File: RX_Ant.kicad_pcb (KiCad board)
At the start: 2 copper layers, 100 x 100 mm, 1705 parts, among them J1 CONN_COAXIAL, J10 CONN_COAXIAL, J11 CONN_01X06, J12 CONN_01X05, J13 CONN_COAXIAL, J14 CONN_COAXIAL, J15 CONN_COAXIAL, J16 CONN_01X01, J17 CONN_01X01, J18 CONN_01X01, J19 CONN_01X01, J2 CONN_COAXIAL, J20 CONN_01X01, J21 CONN_01X01, J22 CONN_01X01, J23 CONN_01X01, J24 CONN_COAXIAL, J25 CONN_COAXIAL, J26 CONN_COAXIAL, J27 CONN_COAXIAL, J28 CONN_COAXIAL, J29 CONN_COAXIAL, J3 CONN_COAXIAL, J30 CONN_COAXIAL, J31 CONN_COAXIAL, J32 CONN_COAXIAL, J33 CONN_COAXIAL, J34 CONN_COAXIAL, J35 CONN_COAXIAL, J36 CONN_COAXIAL, J4 CONN_COAXIAL, J5 CONN_COAXIAL, J6 CONN_COAXIAL, J7 CONN_COAXIAL, J8 CONN_COAXIAL, J9 CONN_COAXIAL

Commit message: stiching again, new gerber
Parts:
- removed the REF** at (117.0, 113.0)
- removed the REF** at (116.0, 113.0)
- removed the REF** at (117.0, 112.0)
- removed the REF** at (116.0, 112.0)
- removed the REF** at (117.0, 111.0)
- removed the REF** at (116.0, 111.0)
- removed the REF** at (115.0, 113.0)
- removed the REF** at (114.0, 113.0)
- removed the REF** at (113.0, 113.0)
- removed the REF** at (112.0, 113.0)
- removed the REF** at (111.0, 113.0)
- removed the REF** at (110.0, 113.0)
- removed the REF** at (109.0, 113.0)
- removed the REF** at (115.0, 112.0)
- removed the REF** at (114.0, 112.0)
- removed the REF** at (113.0, 112.0)
- removed the REF** at (112.0, 112.0)
- removed the REF** at (111.0, 112.0)
- removed the REF** at (110.0, 112.0)
- removed the REF** at (109.0, 112.0)
- removed the REF** at (115.0, 111.0)
- removed the REF** at (114.0, 111.0)
- removed the REF** at (113.0, 111.0)
- removed the REF** at (112.0, 111.0)
- removed the REF** at (111.0, 111.0)
- removed the REF** at (110.0, 111.0)
- removed the REF** at (109.0, 111.0)
- removed the REF** at (101.0, 113.0)
- removed the REF** at (100.0, 113.0)
- removed the REF** at (99.0, 113.0)
- removed the REF** at (98.0, 113.0)
- removed the REF** at (97.0, 113.0)
- removed the REF** at (96.0, 113.0)
- removed the REF** at (95.0, 113.0)
- removed the REF** at (94.0, 113.0)
- removed the REF** at (101.0, 112.0)
- removed the REF** at (100.0, 112.0)
- removed the REF** at (99.0, 112.0)
- removed the REF** at (98.0, 112.0)
- removed the REF** at (97.0, 112.0)
- removed the REF** at (96.0, 112.0)
- removed the REF** at (95.0, 112.0)
- removed the REF** at (94.0, 112.0)
- removed the REF** at (101.0, 111.0)
- removed the REF** at (100.0, 111.0)
- removed the REF** at (99.0, 111.0)
- removed the REF** at (98.0, 111.0)
- removed the REF** at (97.0, 111.0)
- removed the REF** at (96.0, 111.0)
- removed the REF** at (95.0, 111.0)
- removed the REF** at (94.0, 111.0)
- removed the REF** at (86.0, 113.0)
- removed the REF** at (85.0, 113.0)
- removed the REF** at (84.0, 113.0)
- removed the REF** at (83.0, 113.0)
- removed the REF** at (82.0, 113.0)
- removed the REF** at (81.0, 113.0)
- removed the REF** at (80.0, 113.0)
- removed the REF** at (79.0, 113.0)
- removed the REF** at (86.0, 112.0)
- removed the REF** at (85.0, 112.0)
- removed the REF** at (84.0, 112.0)
- removed the REF** at (83.0, 112.0)
- removed the REF** at (82.0, 112.0)
- removed the REF** at (81.0, 112.0)
- removed the REF** at (80.0, 112.0)
- removed the REF** at (79.0, 112.0)
- removed the REF** at (86.0, 111.0)
- removed the REF** at (85.0, 111.0)
- removed the REF** at (84.0, 111.0)
- removed the REF** at (83.0, 111.0)
- removed the REF** at (82.0, 111.0)
- removed the REF** at (81.0, 111.0)
- removed the REF** at (80.0, 111.0)
- removed the REF** at (79.0, 111.0)
- removed the REF** at (71.0, 113.0)
- removed the REF** at (70.0, 113.0)
- removed the REF** at (69.0, 113.0)
- removed the REF** at (68.0, 113.0)
- removed the REF** at (67.0, 113.0)
- removed the REF** at (66.0, 113.0)
- removed the REF** at (65.0, 113.0)
- removed the REF** at (64.0, 113.0)
- removed the REF** at (71.0, 112.0)
- removed the REF** at (70.0, 112.0)
- removed the REF** at (69.0, 112.0)
- removed the REF** at (68.0, 112.0)
- removed the REF** at (67.0, 112.0)
- removed the REF** at (66.0, 112.0)
- removed the REF** at (65.0, 112.0)
- removed the REF** at (64.0, 112.0)
- removed the REF** at (71.0, 111.0)
- removed the REF** at (70.0, 111.0)
- removed the REF** at (69.0, 111.0)
- removed the REF** at (68.0, 111.0)
- removed the REF** at (67.0, 111.0)
- removed the REF** at (66.0, 111.0)
- removed the REF** at (65.0, 111.0)
- removed the REF** at (64.0, 111.0)
- removed the REF** at (56.0, 113.0)
- removed the REF** at (55.0, 113.0)
- removed the REF** at (54.0, 113.0)
- removed the REF** at (53.0, 113.0)
- removed the REF** at (52.0, 113.0)
- removed the REF** at (51.0, 113.0)
- removed the REF** at (50.0, 113.0)
- removed the REF** at (49.0, 113.0)
- removed the REF** at (56.0, 112.0)
- removed the REF** at (55.0, 112.0)
- removed the REF** at (54.0, 112.0)
- removed the REF** at (53.0, 112.0)
- removed the REF** at (52.0, 112.0)
- removed the REF** at (51.0, 112.0)
- removed the REF** at (50.0, 112.0)
- removed the REF** at (49.0, 112.0)
- removed the REF** at (56.0, 111.0)
- removed the REF** at (55.0, 111.0)
- removed the REF** at (54.0, 111.0)
- removed the REF** at (53.0, 111.0)
- removed the REF** at (52.0, 111.0)
- removed the REF** at (51.0, 111.0)
- removed the REF** at (50.0, 111.0)
- removed the REF** at (49.0, 111.0)
- removed the REF** at (41.0, 113.0)
- removed the REF** at (40.0, 113.0)
- removed the REF** at (39.0, 113.0)
- removed the REF** at (38.0, 113.0)
- removed the REF** at (37.0, 113.0)
- removed the REF** at (36.0, 113.0)
- removed the REF** at (35.0, 113.0)
- removed the REF** at (34.0, 113.0)
- removed the REF** at (33.0, 113.0)
- removed the REF** at (32.0, 113.0)
- removed the REF** at (31.0, 113.0)
- removed the REF** at (30.0, 113.0)
- removed the REF** at (29.0, 113.0)
- removed the REF** at (28.0, 113.0)
- removed the REF** at (27.0, 113.0)
- removed the REF** at (41.0, 112.0)
- removed the REF** at (40.0, 112.0)
- removed the REF** at (39.0, 112.0)
- removed the REF** at (38.0, 112.0)
- removed the REF** at (37.0, 112.0)
- removed the REF** at (36.0, 112.0)
- removed the REF** at (35.0, 112.0)
- removed the REF** at (34.0, 112.0)
- removed the REF** at (33.0, 112.0)
- removed the REF** at (32.0, 112.0)
- removed the REF** at (31.0, 112.0)
- removed the REF** at (30.0, 112.0)
- removed the REF** at (29.0, 112.0)
- removed the REF** at (28.0, 112.0)
- removed the REF** at (27.0, 112.0)
- removed the REF** at (41.0, 111.0)
- removed the REF** at (40.0, 111.0)
- removed the REF** at (39.0, 111.0)
- removed the REF** at (38.0, 111.0)
- removed the REF** at (37.0, 111.0)
- removed the REF** at (36.0, 111.0)
- removed the REF** at (35.0, 111.0)
- removed the REF** at (34.0, 111.0)
- removed the REF** at (33.0, 111.0)
- removed the REF** at (32.0, 111.0)
- removed the REF** at (31.0, 111.0)
- removed the REF** at (30.0, 111.0)
- removed the REF** at (29.0, 111.0)
- removed the REF** at (28.0, 111.0)
- removed the REF** at (27.0, 111.0)

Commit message: stiching again, new gerber
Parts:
- added REF**: via, via:via, F.Cu at (111.0, 124.0)
- added REF**: via, via:via, F.Cu at (83.0, 124.0)
- added REF**: via, via:via, F.Cu at (82.0, 124.0)
- added REF**: via, via:via, F.Cu at (81.0, 124.0)
- added REF**: via, via:via, F.Cu at (84.0, 123.0)
- added REF**: via, via:via, F.Cu at (83.0, 123.0)
- added REF**: via, via:via, F.Cu at (82.0, 123.0)
- added REF**: via, via:via, F.Cu at (69.0, 124.0)
- added REF**: via, via:via, F.Cu at (68.0, 124.0)
- added REF**: via, via:via, F.Cu at (67.0, 124.0)
- added REF**: via, via:via, F.Cu at (66.0, 124.0)
- added REF**: via, via:via, F.Cu at (99.0, 124.0)
- added REF**: via, via:via, F.Cu at (69.0, 123.0)
- added REF**: via, via:via, F.Cu at (68.0, 123.0)
- added REF**: via, via:via, F.Cu at (67.0, 123.0)
- added REF**: via, via:via, F.Cu at (54.0, 124.0)
- added REF**: via, via:via, F.Cu at (53.0, 124.0)
- added REF**: via, via:via, F.Cu at (52.0, 124.0)
- added REF**: via, via:via, F.Cu at (51.0, 124.0)
- added REF**: via, via:via, F.Cu at (54.0, 123.0)
- added REF**: via, via:via, F.Cu at (53.0, 123.0)
- added REF**: via, via:via, F.Cu at (52.0, 123.0)
- added REF**: via, via:via, F.Cu at (98.0, 124.0)
- added REF**: via, via:via, F.Cu at (38.0, 124.0)
- added REF**: via, via:via, F.Cu at (37.0, 124.0)
- added REF**: via, via:via, F.Cu at (36.0, 124.0)
- added REF**: via, via:via, F.Cu at (35.0, 124.0)
- added REF**: via, via:via, F.Cu at (34.0, 124.0)
- added REF**: via, via:via, F.Cu at (33.0, 124.0)
- added REF**: via, via:via, F.Cu at (32.0, 124.0)
- added REF**: via, via:via, F.Cu at (31.0, 124.0)
- added REF**: via, via:via, F.Cu at (30.0, 124.0)
- added REF**: via, via:via, F.Cu at (29.0, 124.0)
- added REF**: via, via:via, F.Cu at (97.0, 124.0)
- added REF**: via, via:via, F.Cu at (38.0, 123.0)
- added REF**: via, via:via, F.Cu at (37.0, 123.0)
- added REF**: via, via:via, F.Cu at (36.0, 123.0)
- added REF**: via, via:via, F.Cu at (35.0, 123.0)
- added REF**: via, via:via, F.Cu at (34.0, 123.0)
- added REF**: via, via:via, F.Cu at (33.0, 123.0)
- added REF**: via, via:via, F.Cu at (32.0, 123.0)
- added REF**: via, via:via, F.Cu at (31.0, 123.0)
- added REF**: via, via:via, F.Cu at (30.0, 123.0)
- added REF**: via, via:via, F.Cu at (111.0, 123.0)
- added REF**: via, via:via, F.Cu at (96.0, 124.0)
- added REF**: via, via:via, F.Cu at (96.0, 123.0)
- added REF**: via, via:via, F.Cu at (81.0, 123.0)
- added REF**: via, via:via, F.Cu at (66.0, 123.0)
- added REF**: via, via:via, F.Cu at (51.0, 123.0)
- added REF**: via, via:via, F.Cu at (29.0, 123.0)
- added REF**: via, via:via, F.Cu at (99.0, 123.0)
- added REF**: via, via:via, F.Cu at (98.0, 123.0)
- added REF**: via, via:via, F.Cu at (97.0, 123.0)
- added REF**: via, via:via, F.Cu at (84.0, 124.0)

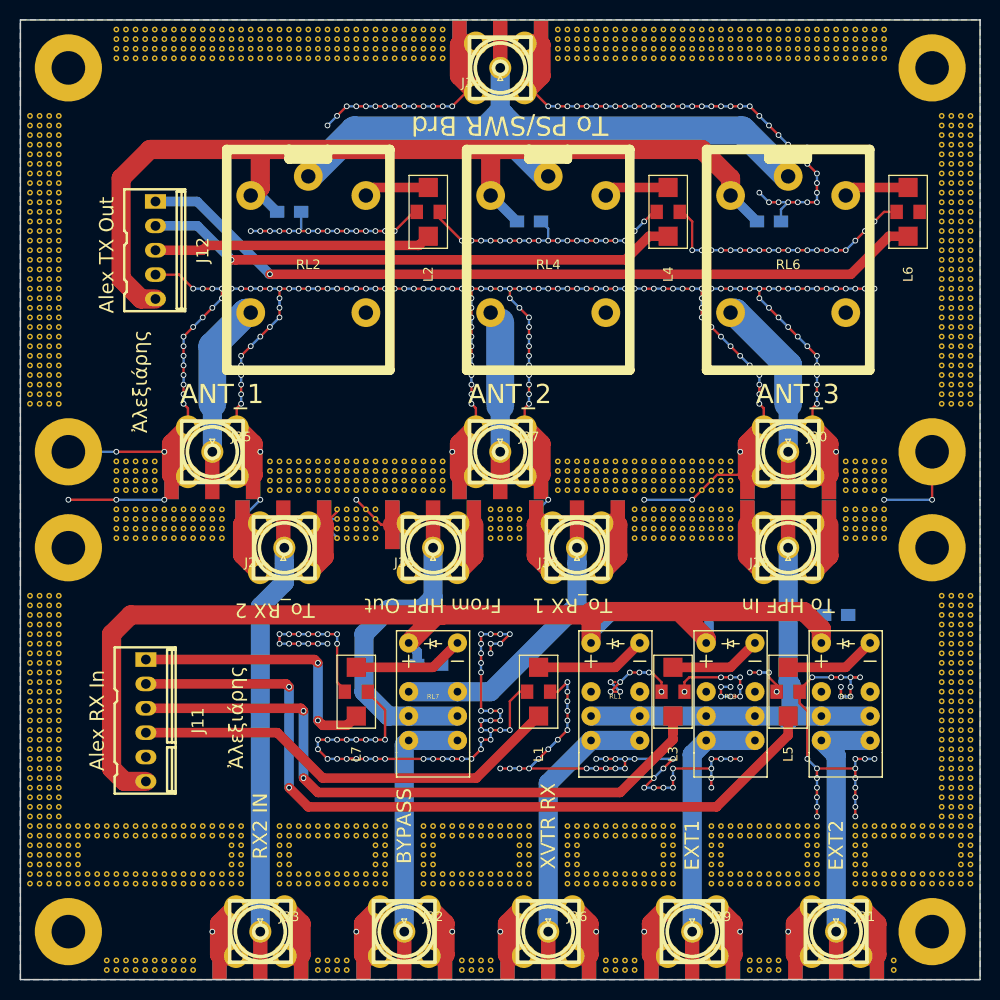
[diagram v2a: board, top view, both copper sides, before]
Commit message: PS_In relay added, new routing V2
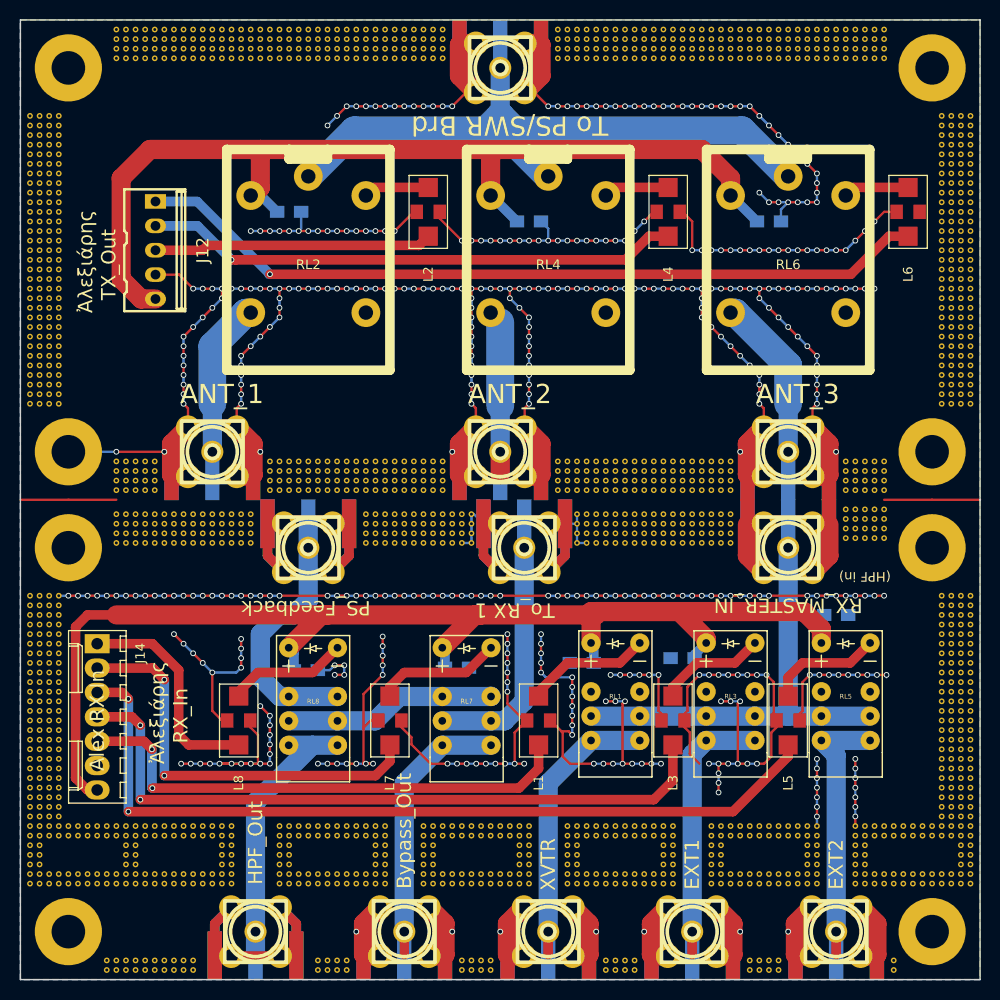
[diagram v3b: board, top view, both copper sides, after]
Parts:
- removed J33, J36: CONN_COAXIAL, Connector_Coaxial:SMA_Amphenol_132289_EdgeMount
- removed J7: CONN_COAXIAL, conn_rf:sma_straight_32k101-400l5
- removed the REF** at (90.0, 77.0)
- removed the REF** at (89.0, 77.0)
- removed the REF** at (88.0, 77.0)
- removed the REF** at (87.0, 77.0)
- removed the REF** at (86.0, 77.0)
- removed the REF** at (85.0, 77.0)
- removed the REF** at (24.0, 113.0)
- removed the REF** at (23.0, 113.0)
- removed the REF** at (24.0, 112.0)
- removed the REF** at (23.0, 112.0)
- removed the REF** at (84.0, 77.0)
- removed the REF** at (24.0, 111.0)
- removed the REF** at (23.0, 111.0)
- removed the REF** at (94.0, 76.0)
- removed the REF** at (93.0, 76.0)
- removed the REF** at (92.0, 76.0)
- removed the REF** at (91.0, 76.0)
- removed the REF** at (90.0, 76.0)
- removed the REF** at (89.0, 76.0)
- removed the REF** at (88.0, 76.0)
- removed the REF** at (87.0, 76.0)
- removed the REF** at (86.0, 76.0)
- removed the REF** at (85.0, 76.0)
- removed the REF** at (72.0, 79.0)
- removed the REF** at (71.0, 79.0)
- removed the REF** at (70.0, 79.0)
- removed the REF** at (69.0, 79.0)
- removed the REF** at (72.0, 78.0)
- removed the REF** at (71.0, 78.0)
- removed the REF** at (70.0, 78.0)
- removed the REF** at (69.0, 78.0)
- removed the REF** at (72.0, 77.0)
- removed the REF** at (71.0, 77.0)
- removed the REF** at (70.0, 77.0)
- removed the REF** at (69.0, 77.0)
- removed the REF** at (72.0, 76.0)
- removed the REF** at (71.0, 76.0)
- removed the REF** at (70.0, 76.0)
- removed the REF** at (41.0, 79.0)
- removed the REF** at (40.0, 79.0)
- removed the REF** at (39.0, 79.0)
- removed the REF** at (38.0, 79.0)
- removed the REF** at (37.0, 79.0)
- removed the REF** at (36.0, 79.0)
- removed the REF** at (35.0, 79.0)
- removed the REF** at (34.0, 79.0)
- removed the REF** at (33.0, 79.0)
- removed the REF** at (32.0, 79.0)
- removed the REF** at (31.0, 79.0)
- removed the REF** at (30.0, 79.0)
- removed the REF** at (41.0, 78.0)
- removed the REF** at (40.0, 78.0)
- removed the REF** at (39.0, 78.0)
- removed the REF** at (38.0, 78.0)
- removed the REF** at (37.0, 78.0)
- removed the REF** at (36.0, 78.0)
- removed the REF** at (35.0, 78.0)
- removed the REF** at (34.0, 78.0)
- removed the REF** at (33.0, 78.0)
- removed the REF** at (32.0, 78.0)
- removed the REF** at (31.0, 78.0)
- removed the REF** at (30.0, 78.0)
- removed the REF** at (41.0, 77.0)
- removed the REF** at (40.0, 77.0)
- removed the REF** at (39.0, 77.0)
- removed the REF** at (38.0, 77.0)
- removed the REF** at (37.0, 77.0)
- removed the REF** at (36.0, 77.0)
- removed the REF** at (35.0, 77.0)
- removed the REF** at (34.0, 77.0)
- removed the REF** at (33.0, 77.0)
- removed the REF** at (32.0, 77.0)
- removed the REF** at (31.0, 77.0)
- removed the REF** at (30.0, 77.0)
- removed the REF** at (41.0, 76.0)
- removed the REF** at (40.0, 76.0)
- removed the REF** at (39.0, 76.0)
- removed the REF** at (38.0, 76.0)
- removed the REF** at (37.0, 76.0)
- removed the REF** at (36.0, 76.0)
- removed the REF** at (35.0, 76.0)
- removed the REF** at (34.0, 76.0)
- removed the REF** at (33.0, 76.0)
- removed the REF** at (32.0, 76.0)
- removed the REF** at (31.0, 76.0)
- removed the REF** at (69.0, 76.0)
- removed the REF** at (53.0, 76.0)
- removed the REF** at (30.0, 76.0)
- removed the REF** at (84.0, 76.0)
- removed the REF** at (57.0, 79.0)
- removed the REF** at (56.0, 79.0)
- removed the REF** at (55.0, 79.0)
- removed the REF** at (54.0, 79.0)
- removed the REF** at (53.0, 79.0)
- removed the REF** at (57.0, 78.0)
- removed the REF** at (56.0, 78.0)
- removed the REF** at (55.0, 78.0)
- removed the REF** at (54.0, 78.0)
- removed the REF** at (53.0, 78.0)
- removed the REF** at (57.0, 77.0)
- removed the REF** at (56.0, 77.0)
- removed the REF** at (55.0, 77.0)
- removed the REF** at (43.0, 115.0)
- removed the REF** at (54.0, 77.0)
- removed the REF** at (53.0, 77.0)
- removed the REF** at (43.0, 114.0)
- removed the REF** at (57.0, 76.0)
- removed the REF** at (56.0, 76.0)
- removed the REF** at (43.0, 113.0)
- removed the REF** at (26.0, 113.0)
- removed the REF** at (25.0, 113.0)
- removed the REF** at (43.0, 112.0)
- removed the REF** at (55.0, 76.0)
- removed the REF** at (26.0, 112.0)
- removed the REF** at (25.0, 112.0)
- removed the REF** at (43.0, 111.0)
- removed the REF** at (26.0, 111.0)
- removed the REF** at (25.0, 111.0)
- removed the REF** at (43.0, 110.0)
- removed the REF** at (54.0, 76.0)
- removed the REF** at (94.0, 79.0)
- removed the REF** at (43.0, 109.0)
- removed the REF** at (93.0, 79.0)
- removed the REF** at (92.0, 79.0)
- removed the REF** at (91.0, 79.0)
- removed the REF** at (90.0, 79.0)
- removed the REF** at (89.0, 79.0)
- removed the REF** at (88.0, 79.0)
- removed the REF** at (87.0, 79.0)
- removed the REF** at (86.0, 79.0)
- removed the REF** at (85.0, 79.0)
- removed the REF** at (84.0, 79.0)
- removed the REF** at (94.0, 78.0)
- removed the REF** at (93.0, 78.0)
- removed the REF** at (92.0, 78.0)
- removed the REF** at (91.0, 78.0)
- removed the REF** at (90.0, 78.0)
- removed the REF** at (89.0, 78.0)
- removed the REF** at (88.0, 78.0)
- removed the REF** at (87.0, 78.0)
- removed the REF** at (86.0, 78.0)
- removed the REF** at (85.0, 78.0)
- removed the REF** at (84.0, 78.0)
- removed the REF** at (94.0, 77.0)
- removed the REF** at (93.0, 77.0)
- removed the REF** at (92.0, 77.0)
- removed the REF** at (91.0, 77.0)
- added C2: 100n, Capacitors_SMD:C_0805_HandSoldering, B.Cu at (49.8, 92.8)
- added J37: CONN_COAXIAL, conn_rf:sma_straight_32k101-400l5, F.Cu at (44.5, 120.0)
- added L8: L_cap, Ferrite_LC_NFM41P:Ferrite_LC_NFM41P, F.Cu at (42.8, 98.0)
- added REF**: via, via:via, F.Cu at (67.0, 79.5)
- added REF**: via, via:via, F.Cu at (64.0, 76.5)
- added REF**: via, via:via, F.Cu at (90.0, 79.5)
- added REF**: via, via:via, F.Cu at (40.0, 79.5)
- added REF**: via, via:via, F.Cu at (40.0, 78.5)
- added REF**: via, via:via, F.Cu at (40.0, 77.5)
- added REF**: via, via:via, F.Cu at (40.0, 76.5)
- added REF**: via, via:via, F.Cu at (39.0, 79.5)
- added REF**: via, via:via, F.Cu at (38.0, 79.5)
- added REF**: via, via:via, F.Cu at (37.0, 79.5)
- added REF**: via, via:via, F.Cu at (36.0, 79.5)
- added REF**: via, via:via, F.Cu at (39.0, 78.5)
- added REF**: via, via:via, F.Cu at (65.0, 77.5)
- added REF**: via, via:via, F.Cu at (38.0, 78.5)
- added REF**: via, via:via, F.Cu at (37.0, 78.5)
- added REF**: via, via:via, F.Cu at (36.0, 78.5)
- added REF**: via, via:via, F.Cu at (39.0, 77.5)
- added REF**: via, via:via, F.Cu at (38.0, 77.5)
- added REF**: via, via:via, F.Cu at (37.0, 77.5)
- added REF**: via, via:via, F.Cu at (36.0, 77.5)
- added REF**: via, via:via, F.Cu at (39.0, 76.5)
- added REF**: via, via:via, F.Cu at (38.0, 76.5)
- added REF**: via, via:via, F.Cu at (37.0, 76.5)
- added REF**: via, via:via, F.Cu at (64.0, 77.5)
- added REF**: via, via:via, F.Cu at (36.0, 76.5)
- added REF**: via, via:via, F.Cu at (35.0, 76.5)
- added REF**: via, via:via, F.Cu at (30.0, 76.5)
- added REF**: via, via:via, F.Cu at (31.0, 76.5)
- added REF**: via, via:via, F.Cu at (32.0, 76.5)
- added REF**: via, via:via, F.Cu at (33.0, 76.5)
- added REF**: via, via:via, F.Cu at (34.0, 76.5)
- added REF**: via, via:via, F.Cu at (35.0, 77.5)
- added REF**: via, via:via, F.Cu at (30.0, 77.5)
- added REF**: via, via:via, F.Cu at (31.0, 77.5)
- added REF**: via, via:via, F.Cu at (65.0, 78.5)
- added REF**: via, via:via, F.Cu at (32.0, 77.5)
- added REF**: via, via:via, F.Cu at (33.0, 77.5)
- added REF**: via, via:via, F.Cu at (34.0, 77.5)
- added REF**: via, via:via, F.Cu at (35.0, 78.5)
- added REF**: via, via:via, F.Cu at (30.0, 78.5)
- added REF**: via, via:via, F.Cu at (31.0, 78.5)
- added REF**: via, via:via, F.Cu at (32.0, 78.5)
- added REF**: via, via:via, F.Cu at (33.0, 78.5)
- added REF**: via, via:via, F.Cu at (34.0, 78.5)
- added REF**: via, via:via, F.Cu at (35.0, 79.5)
- added REF**: via, via:via, F.Cu at (64.0, 78.5)
- added REF**: via, via:via, F.Cu at (30.0, 79.5)
- added REF**: via, via:via, F.Cu at (31.0, 79.5)
- added REF**: via, via:via, F.Cu at (32.0, 79.5)
- added REF**: via, via:via, F.Cu at (33.0, 79.5)
- added REF**: via, via:via, F.Cu at (34.0, 79.5)
- added REF**: via, via:via, F.Cu at (94.0, 79.5)
- added REF**: via, via:via, F.Cu at (93.0, 79.5)
- added REF**: via, via:via, F.Cu at (92.0, 79.5)
- added REF**: via, via:via, F.Cu at (91.0, 79.5)
- added REF**: via, via:via, F.Cu at (94.0, 78.5)
- added REF**: via, via:via, F.Cu at (65.0, 79.5)
- added REF**: via, via:via, F.Cu at (93.0, 78.5)
- added REF**: via, via:via, F.Cu at (92.0, 78.5)
- added REF**: via, via:via, F.Cu at (91.0, 78.5)
- added REF**: via, via:via, F.Cu at (94.0, 77.5)
- added REF**: via, via:via, F.Cu at (93.0, 77.5)
- added REF**: via, via:via, F.Cu at (92.0, 77.5)
- added REF**: via, via:via, F.Cu at (91.0, 77.5)
- added REF**: via, via:via, F.Cu at (94.0, 76.5)
- added REF**: via, via:via, F.Cu at (93.0, 76.5)
- added REF**: via, via:via, F.Cu at (92.0, 76.5)
- added REF**: via, via:via, F.Cu at (64.0, 79.5)
- added REF**: via, via:via, F.Cu at (91.0, 76.5)
- added REF**: via, via:via, F.Cu at (44.0, 79.5)
- added REF**: via, via:via, F.Cu at (43.0, 79.5)
- added REF**: via, via:via, F.Cu at (42.0, 79.5)
- added REF**: via, via:via, F.Cu at (41.0, 79.5)
- added REF**: via, via:via, F.Cu at (44.0, 78.5)
- added REF**: via, via:via, F.Cu at (43.0, 78.5)
- added REF**: via, via:via, F.Cu at (42.0, 78.5)
- added REF**: via, via:via, F.Cu at (41.0, 78.5)
- added REF**: via, via:via, F.Cu at (44.0, 77.5)
- added REF**: via, via:via, F.Cu at (60.0, 79.5)
- added REF**: via, via:via, F.Cu at (43.0, 77.5)
- added REF**: via, via:via, F.Cu at (42.0, 77.5)
- added REF**: via, via:via, F.Cu at (41.0, 77.5)
- added REF**: via, via:via, F.Cu at (44.0, 76.5)
- added REF**: via, via:via, F.Cu at (43.0, 76.5)
- added REF**: via, via:via, F.Cu at (42.0, 76.5)
- added REF**: via, via:via, F.Cu at (41.0, 76.5)
- added REF**: via, via:via, F.Cu at (59.0, 79.5)
- added REF**: via, via:via, F.Cu at (31.0, 111.0)
- added REF**: via, via:via, F.Cu at (31.0, 112.0)
- added REF**: via, via:via, F.Cu at (31.0, 113.0)
- added REF**: via, via:via, F.Cu at (58.0, 79.5)
- added REF**: via, via:via, F.Cu at (66.0, 79.5)
- added REF**: via, via:via, F.Cu at (57.0, 79.5)
- added REF**: via, via:via, F.Cu at (56.0, 79.5)
- added REF**: via, via:via, F.Cu at (61.0, 79.5)
- added REF**: via, via:via, F.Cu at (41.0, 113.0)
- added REF**: via, via:via, F.Cu at (32.0, 113.0)
- added REF**: via, via:via, F.Cu at (41.0, 112.0)
- added REF**: via, via:via, F.Cu at (32.0, 112.0)
- added REF**: via, via:via, F.Cu at (60.0, 78.5)
- added REF**: via, via:via, F.Cu at (41.0, 111.0)
- added REF**: via, via:via, F.Cu at (32.0, 111.0)
- added REF**: via, via:via, F.Cu at (59.0, 78.5)
- added REF**: via, via:via, F.Cu at (58.0, 78.5)
- added REF**: via, via:via, F.Cu at (57.0, 78.5)
- added REF**: via, via:via, F.Cu at (56.0, 78.5)
- added REF**: via, via:via, F.Cu at (61.0, 78.5)
- added REF**: via, via:via, F.Cu at (60.0, 77.5)
- added REF**: via, via:via, F.Cu at (67.0, 78.5)
- added REF**: via, via:via, F.Cu at (59.0, 77.5)
- added REF**: via, via:via, F.Cu at (58.0, 77.5)
- added REF**: via, via:via, F.Cu at (57.0, 77.5)
- added REF**: via, via:via, F.Cu at (56.0, 77.5)
- added REF**: via, via:via, F.Cu at (61.0, 77.5)
- added REF**: via, via:via, F.Cu at (60.0, 76.5)
- added REF**: via, via:via, F.Cu at (59.0, 76.5)
- added REF**: via, via:via, F.Cu at (58.0, 76.5)
- added REF**: via, via:via, F.Cu at (57.0, 76.5)
- added REF**: via, via:via, F.Cu at (56.0, 76.5)
- added REF**: via, via:via, F.Cu at (66.0, 78.5)
- added REF**: via, via:via, F.Cu at (61.0, 76.5)
- added REF**: via, via:via, F.Cu at (62.0, 76.5)
- added REF**: via, via:via, F.Cu at (63.0, 76.5)
- added REF**: via, via:via, F.Cu at (62.0, 77.5)
- added REF**: via, via:via, F.Cu at (63.0, 77.5)
- added REF**: via, via:via, F.Cu at (62.0, 78.5)
- added REF**: via, via:via, F.Cu at (63.0, 78.5)
- added REF**: via, via:via, F.Cu at (62.0, 79.5)
- added REF**: via, via:via, F.Cu at (63.0, 79.5)
- added REF**: via, via:via, F.Cu at (78.0, 76.5)
- added REF**: via, via:via, F.Cu at (67.0, 77.5)
- added REF**: via, via:via, F.Cu at (78.0, 77.5)
- added REF**: via, via:via, F.Cu at (78.0, 78.5)
- added REF**: via, via:via, F.Cu at (78.0, 79.5)
- added REF**: via, via:via, F.Cu at (83.0, 76.5)
- added REF**: via, via:via, F.Cu at (84.0, 76.5)
- added REF**: via, via:via, F.Cu at (85.0, 76.5)
- added REF**: via, via:via, F.Cu at (86.0, 76.5)
- added REF**: via, via:via, F.Cu at (83.0, 77.5)
- added REF**: via, via:via, F.Cu at (84.0, 77.5)
- added REF**: via, via:via, F.Cu at (85.0, 77.5)
- added REF**: via, via:via, F.Cu at (66.0, 77.5)
- added REF**: via, via:via, F.Cu at (86.0, 77.5)
- added REF**: via, via:via, F.Cu at (83.0, 78.5)
- added REF**: via, via:via, F.Cu at (84.0, 78.5)
- added REF**: via, via:via, F.Cu at (85.0, 78.5)
- added REF**: via, via:via, F.Cu at (86.0, 78.5)
- added REF**: via, via:via, F.Cu at (83.0, 79.5)
- added REF**: via, via:via, F.Cu at (84.0, 79.5)
- added REF**: via, via:via, F.Cu at (85.0, 79.5)
- added REF**: via, via:via, F.Cu at (86.0, 79.5)
- added REF**: via, via:via, F.Cu at (82.0, 79.5)
- added REF**: via, via:via, F.Cu at (67.0, 76.5)
- added REF**: via, via:via, F.Cu at (81.0, 79.5)
- added REF**: via, via:via, F.Cu at (80.0, 79.5)
- added REF**: via, via:via, F.Cu at (79.0, 79.5)
- added REF**: via, via:via, F.Cu at (82.0, 78.5)
- added REF**: via, via:via, F.Cu at (81.0, 78.5)
- added REF**: via, via:via, F.Cu at (80.0, 78.5)
- added REF**: via, via:via, F.Cu at (79.0, 78.5)
- added REF**: via, via:via, F.Cu at (82.0, 77.5)
- added REF**: via, via:via, F.Cu at (81.0, 77.5)
- added REF**: via, via:via, F.Cu at (80.0, 77.5)
- added REF**: via, via:via, F.Cu at (66.0, 76.5)
- added REF**: via, via:via, F.Cu at (79.0, 77.5)
- added REF**: via, via:via, F.Cu at (82.0, 76.5)
- added REF**: via, via:via, F.Cu at (81.0, 76.5)
- added REF**: via, via:via, F.Cu at (80.0, 76.5)
- added REF**: via, via:via, F.Cu at (79.0, 76.5)
- added REF**: via, via:via, F.Cu at (87.0, 76.5)
- added REF**: via, via:via, F.Cu at (88.0, 76.5)
- added REF**: via, via:via, F.Cu at (89.0, 76.5)
- added REF**: via, via:via, F.Cu at (90.0, 76.5)
- added REF**: via, via:via, F.Cu at (87.0, 77.5)
- added REF**: via, via:via, F.Cu at (65.0, 76.5)
- added REF**: via, via:via, F.Cu at (88.0, 77.5)
- added REF**: via, via:via, F.Cu at (89.0, 77.5)
- added REF**: via, via:via, F.Cu at (90.0, 77.5)
- added REF**: via, via:via, F.Cu at (87.0, 78.5)
- added REF**: via, via:via, F.Cu at (88.0, 78.5)
- added REF**: via, via:via, F.Cu at (89.0, 78.5)
- added REF**: via, via:via, F.Cu at (90.0, 78.5)
- added REF**: via, via:via, F.Cu at (87.0, 79.5)
- added REF**: via, via:via, F.Cu at (88.0, 79.5)
- added REF**: via, via:via, F.Cu at (89.0, 79.5)
- added RL8: EC2-12NU, 2_Form_C_Relay:THT_2_formC, F.Cu at (50.5, 95.5)
- J11: value CONN_01X06 -> CONN_COAXIAL; footprint conn_kk100:kk100_22-23-2061 -> Connector_Coaxial:SMA_Amphenol_132289_EdgeMount; moved to B.Cu
- J14: value CONN_COAXIAL -> Conn_01x07; footprint conn_rf:sma_straight_32k101-400l5 -> Connectors_Molex:Molex_KK-6410-07_07x2.54mm_Straight
- J24, J25, J26, J27, J28, J29, J30, J31, J32, J34, J35: moved to B.Cu
- moved J24 45.0 mm to (44.5, 122.5), turned to 270 degrees
- moved J13 40.3 mm to (50.0, 80.0)
- moved J11 26.6 mm to (50.0, 77.5), turned to 90 degrees
- moved J14 21.9 mm to (28.0, 90.0), turned to 270 degrees
- moved J35 9.50 mm to (72.5, 77.5)
- moved J15 9.50 mm to (72.5, 80.0)
- moved C5 6.73 mm to (78.5, 92.0), turned to 0 degrees
- moved C1 6.02 mm to (89.0, 91.5), turned to 0 degrees
- moved L7 4.61 mm to (58.5, 98.0)
- moved RL7 3.54 mm to (66.5, 95.5)
- moved L1 3.00 mm to (74.0, 98.0)
- moved L3 3.00 mm to (88.0, 98.0)
- moved L5 3.00 mm to (100.0, 98.0)
- moved C9 2.92 mm to (65.5, 92.5)
- moved J34 0.10 mm to (70.0, 27.5)
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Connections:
- J11 pad 1: RX_BYPASS_OUT -> Net-(J11-Pad1)
- J11 pad 2: RX3_IN -> GND
- J13 pad 1: Net-(J13-Pad1) -> Net-(J11-Pad1)
- J14 pad 1: Net-(J13-Pad1) -> TX_RX_RLY
- J14 pad 2: GND -> RX_BYPASS_OUT
- J24 pad 1: Net-(J13-Pad1) -> Net-(J24-Pad1)
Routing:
- net GND: track 854.0 -> 979.0 mm, vias 423 -> 470
- net Net-(J13-Pad1): track 45.9 -> 0.00 mm
- net Net-(J11-Pad1): track 0.00 -> 30.3 mm
- net Net-(J24-Pad1): track 0.00 -> 29.5 mm
- net TX_RX_RLY: track 0.00 -> 23.1 mm
- net (no net): track 0.00 -> 20.0 mm
- net RX_BYPASS_OUT: track 28.7 -> 43.3 mm
- net Net-(L8-Pad1): track 0.00 -> 12.6 mm
- net +12V: track 225.8 -> 236.0 mm
- net Xvtr_IN: track 45.6 -> 53.7 mm, vias 0 -> 2
- net Net-(J15-Pad1): track 33.2 -> 25.4 mm
- net Net-(RL7-Pad10): track 29.7 -> 22.2 mm
- net RX3_IN: track 83.5 -> 87.6 mm
- net RX2_IN: track 69.9 -> 72.7 mm
- net Net-(J2-Pad1): track 18.8 -> 16.4 mm
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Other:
- board text added: "(HPF in)"
- board text added: "Bypass_Out"
- board text added: "HPF_Out"
- board text added: "PS_Feedback"
- board text added: "RX_MASTER_IN"
- board text added: "TX_RX_RLY"
- board text added: "XVTR"
- board text added: "Ἀλεξιάρης RX_In"
- board text added: "Ἀλεξιάρης TX_Out"
- board text removed: "Alex TX Out"
- board text removed: "BYPASS"
- board text removed: "From HPF Out"
- board text removed: "RX2 IN"
- board text removed: "To HPF In"
- board text removed: "To_RX 2"
- board text removed: "XVTR RX"
- board text removed: "Ἀλεξιάρης"
